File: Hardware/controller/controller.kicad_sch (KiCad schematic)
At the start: 16 parts, among them J101 Conn_02x10_Odd_Even, J102 Conn_02x10_Odd_Even

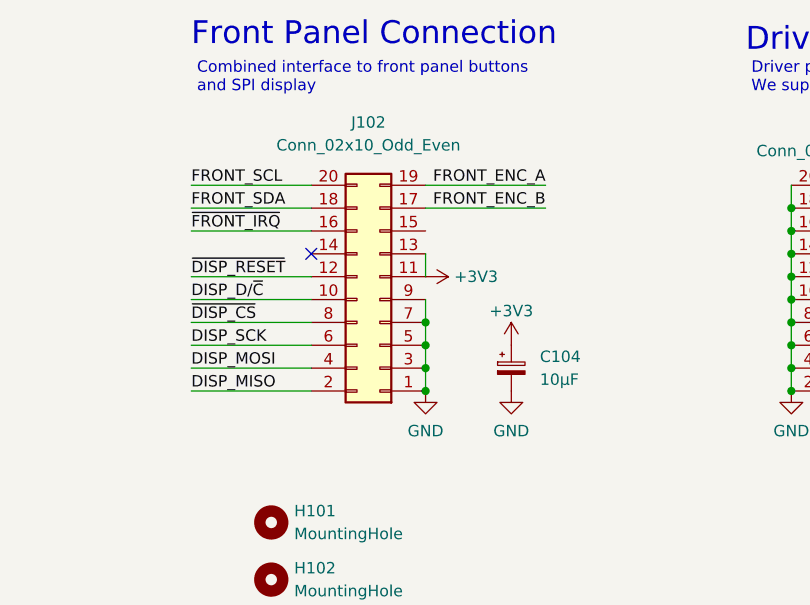
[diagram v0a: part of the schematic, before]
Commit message: Basic controller board finished
- This just has the connections to the front panel and driver board; it
  lacks the rear IO connectors, a power button, and the Ethernet PHY
  currently
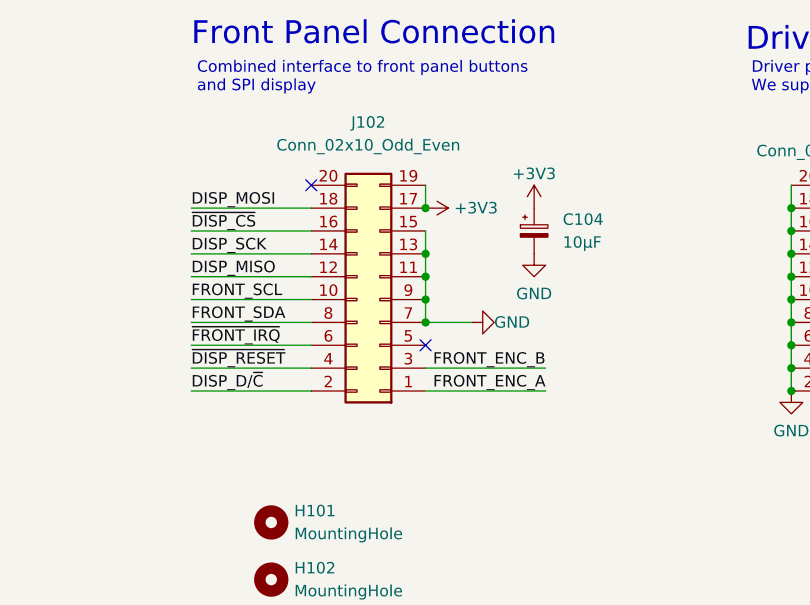
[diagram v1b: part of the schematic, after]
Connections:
- net +3V3: now also J102.17 (Pin_17), J102.19 (Pin_19); no longer J102.11 (Pin_11), J102.13 (Pin_13)
- net DISP_D/~{C}: now also J102.2 (Pin_2); no longer J102.10 (Pin_10)
- net DISP_MISO: now also J102.12 (Pin_12); no longer J102.2 (Pin_2)
- net DISP_MOSI: now also J102.18 (Pin_18); no longer J102.4 (Pin_4)
- net DISP_SCK: now also J102.14 (Pin_14); no longer J102.6 (Pin_6)
- net FRONT_ENC_A: now also J102.1 (Pin_1); no longer J102.19 (Pin_19)
- net FRONT_ENC_B: now also J102.3 (Pin_3); no longer J102.17 (Pin_17)
- net FRONT_SCL: now also J102.10 (Pin_10); no longer J102.20 (Pin_20)
- net FRONT_SDA: now also J102.8 (Pin_8); no longer J102.18 (Pin_18)
- net GND: now also J102.11 (Pin_11), J102.13 (Pin_13), J102.15 (Pin_15); no longer J102.1 (Pin_1), J102.3 (Pin_3), J102.5 (Pin_5)
- net ~{DISP_CS}: now also J102.16 (Pin_16); no longer J102.8 (Pin_8)
- net ~{DISP_RESET}: now also J102.4 (Pin_4); no longer J102.12 (Pin_12)
- net ~{FRONT_IRQ}: now also J102.6 (Pin_6); no longer J102.16 (Pin_16)
- no-connect marks 2 -> 3
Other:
- moved on the sheet: C104

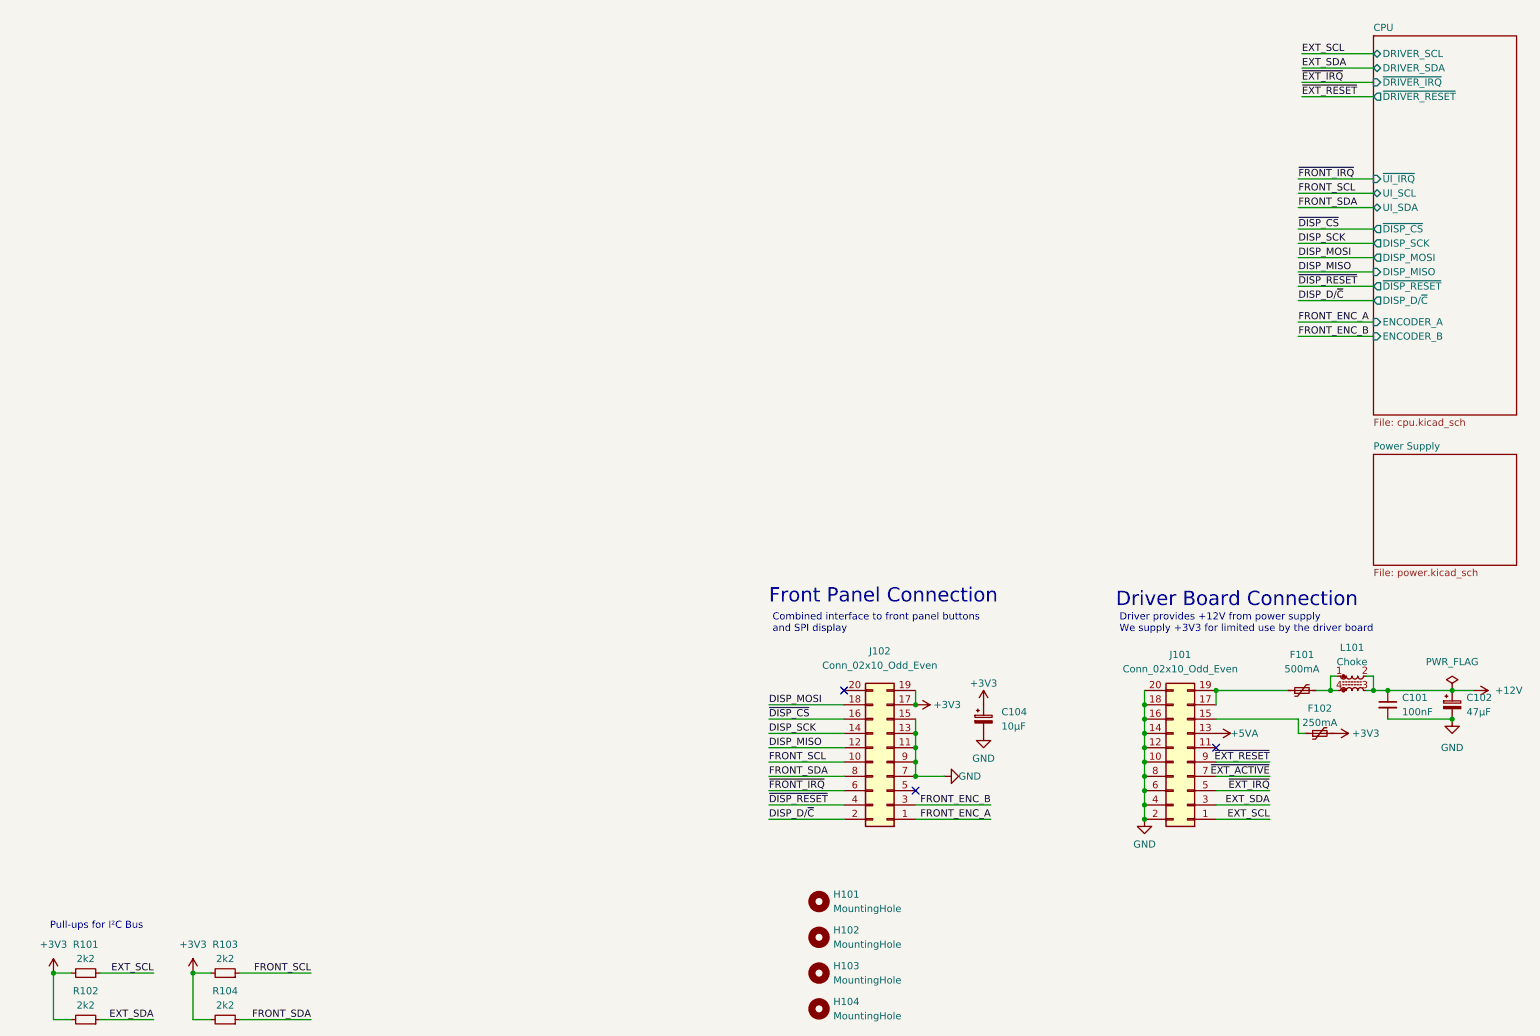
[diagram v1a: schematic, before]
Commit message: Added basic rear IO connector
- Placed the connector for the rear IO board, which will carry USB, I2C,
  Ethernet and power. Currently, USB and I2C have been hooked up.

- Added an I2C switch. This will allow sharing the secondary I2C bus
  between the front panel and rear IO, without needing to worry about
  address conflicts or other such issues.

  Removed the on-board I2C EEPROM; we have a NOR flash instead.
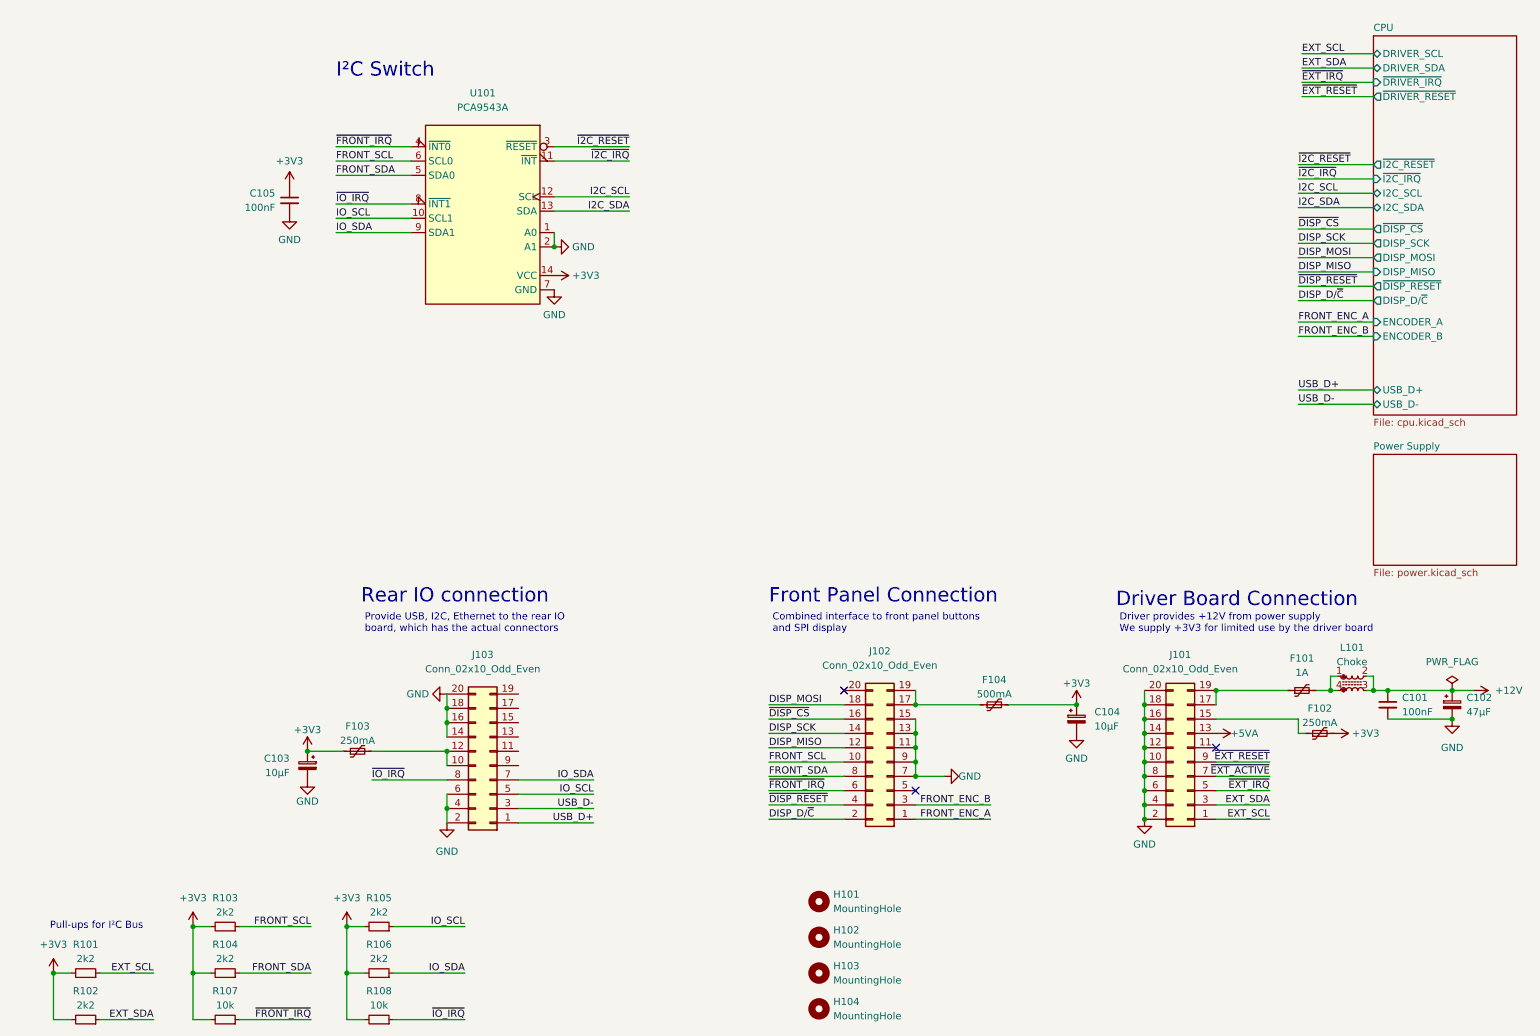
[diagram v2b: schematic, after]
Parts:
- added C103: 10µF, Capacitor_Tantalum_SMD:CP_EIA-3216-18_Kemet-A_Pad1.58x1.35mm_HandSolder, symbol Device:C_Polarized_Small
- added C105: 100nF, Capacitor_SMD:C_0805_2012Metric_Pad1.18x1.45mm_HandSolder, symbol Device:C_Small
- added F103: 250mA, Fuse:Fuse_1206_3216Metric_Pad1.42x1.75mm_HandSolder, symbol Device:Polyfuse_Small
- added F104: 500mA, Fuse:Fuse_1206_3216Metric_Pad1.42x1.75mm_HandSolder, symbol Device:Polyfuse_Small
- added J103: Conn_02x10_Odd_Even, Connector_PinHeader_1.27mm:PinHeader_2x10_P1.27mm_Vertical_SMD, symbol Connector_Generic:Conn_02x10_Odd_Even
- added R105, R106: 2k2, Resistor_SMD:R_0805_2012Metric_Pad1.20x1.40mm_HandSolder, symbol Device:R_Small
- added R107, R108: 10k, Resistor_SMD:R_0805_2012Metric_Pad1.20x1.40mm_HandSolder, symbol Device:R_Small
- added U101: PCA9543A, Package_SO:TSSOP-14_4.4x5mm_P0.65mm, symbol programmable-load:PCA9543A
- F101: value 500mA -> 1A; MPN 0ZCG0050AF2C -> 0ZCG0110BF2B
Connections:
- net +3V3: now also C103.1, C105.1, F103.1, F104.2, R105.2, R106.2, R107.2, R108.2, U101.14 (VCC); no longer J102.17 (Pin_17), J102.19 (Pin_19)
- net FRONT_SCL: now also U101.6 (SCL0)
- net FRONT_SDA: now also U101.5 (SDA0)
- net GND: now also C103.2, C105.2, J103.14 (Pin_14), J103.16 (Pin_16), J103.18 (Pin_18), J103.2 (Pin_2), J103.20 (Pin_20), J103.4 (Pin_4), J103.6 (Pin_6), U101.1 (A0), U101.2 (A1), U101.7 (GND)
- net ~{FRONT_IRQ}: now also R107.1, U101.4 (~{INT0})
- new net: F104.1, J102.17 (Pin_17), J102.19 (Pin_19)
- new net: F103.2, J103.10 (Pin_10), J103.12 (Pin_12)
- new net I2C_SCL: U101.12 (SCL)
- new net I2C_SDA: U101.13 (SDA)
- new net IO_SCL: J103.5 (Pin_5), R105.1, U101.10 (SCL1)
- new net IO_SDA: J103.7 (Pin_7), R106.1, U101.9 (SDA1)
- new net USB_D+: J103.1 (Pin_1)
- new net USB_D-: J103.3 (Pin_3)
- new net ~{I2C_IRQ}: U101.11 (~{INT})
- new net ~{I2C_RESET}: U101.3 (~{RESET})
- new net ~{IO_IRQ}: J103.8 (Pin_8), R108.1, U101.8 (~{INT1})
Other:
- sheet CPU ports: added I2C_SCL, I2C_SDA, USB_D+, USB_D-, ~{I2C_IRQ}, ~{I2C_RESET}; removed UI_SCL, UI_SDA, ~{UI_IRQ}
- note added: "I²C Switch"
- note added: "Provide USB, I2C, Ethernet to the rear IO board, which has the actual connectors"
- note added: "Rear IO connection"
- moved on the sheet: C104, R103, R104

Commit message: Added Ethernet PHY
- Placed the Ethernet PHY on the controller board, and routed its lines
  to the rear panel connector. The MAC address will be stored in the NOR
  flash, and will need to be programmed in. (This avoids the complexity
  of needing a larger I2C switch to give us another bus for an I2C
  EEPROM; though we could ostensibly put one on the rear IO board.)
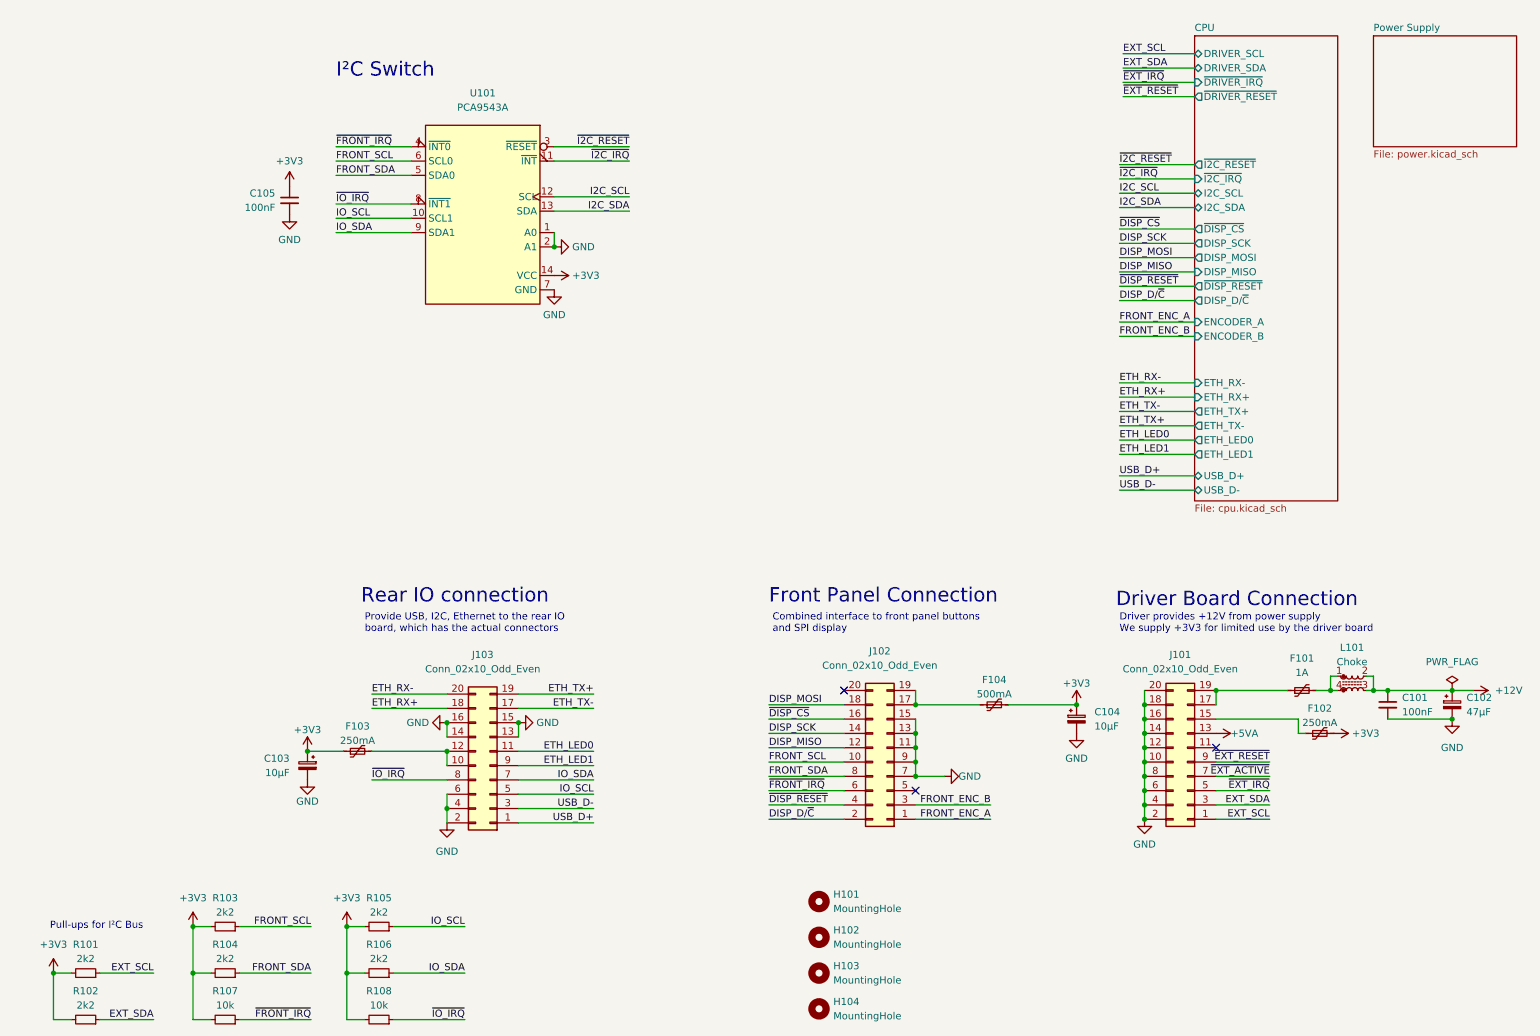
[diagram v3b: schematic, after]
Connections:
- net GND: now also J103.13 (Pin_13), J103.15 (Pin_15); no longer J103.18 (Pin_18), J103.20 (Pin_20)
- net ETH_LED0: now reaches J103.11 (Pin_11)
- net ETH_TX-: now reaches J103.17 (Pin_17)
- net ETH_TX+: now reaches J103.19 (Pin_19)
- net ETH_LED1: now reaches J103.9 (Pin_9)
- new net ETH_RX+: J103.18 (Pin_18)
- new net ETH_RX-: J103.20 (Pin_20)
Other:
- sheet CPU ports: added ETH_LED0, ETH_LED1, ETH_RX+, ETH_RX-, ETH_TX+, ETH_TX-; removed none
- title: (none) -> Programmable Load Controller
